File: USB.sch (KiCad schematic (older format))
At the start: 7 parts

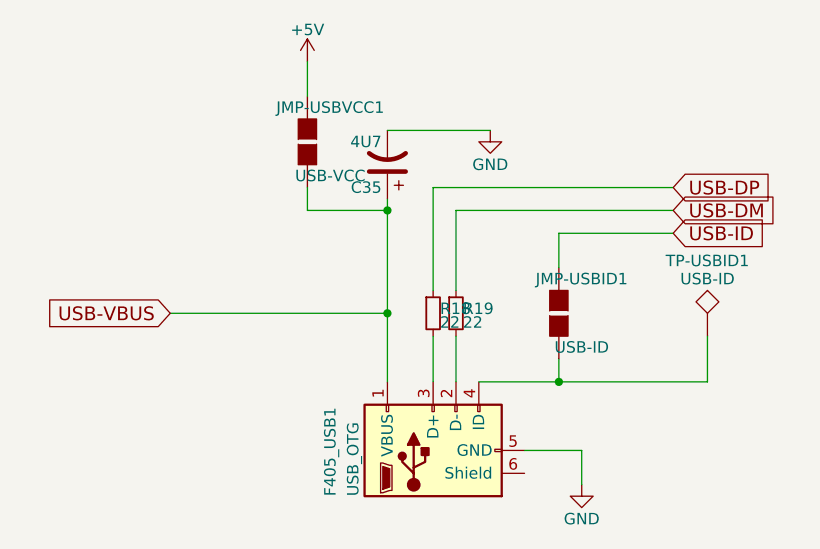
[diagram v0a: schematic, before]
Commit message: tp name fixes
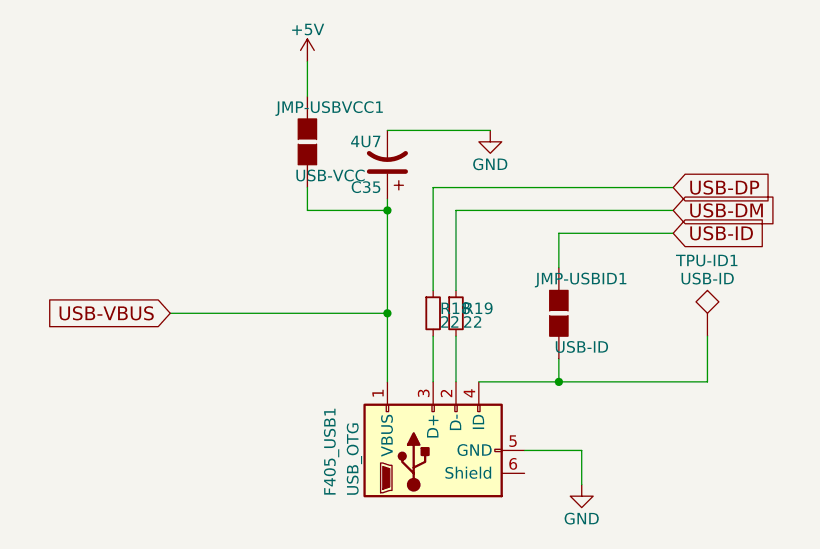
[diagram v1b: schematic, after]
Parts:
- renumbered TP-USBID1 to TPU-ID1
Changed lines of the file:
@@
 $EndComp
 $Comp
-L TEST TP-USBID1
+L TEST TPU-ID1
 U 1 1 5B312B63
 P 7050 3800
-F 0 "TP-USBID1" H 7050 4100 50  0000 C BNN
+F 0 "TPU-ID1" H 7050 4100 50  0000 C BNN
 F 1 "USB-ID" H 7050 4050 50  0000 C CNN
 F 2 "Measurement_Points:Measurement_Point_Round-SMD-Pad_Small" H 7050 3800 50  0001 C CNN

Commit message: Name changes on silk
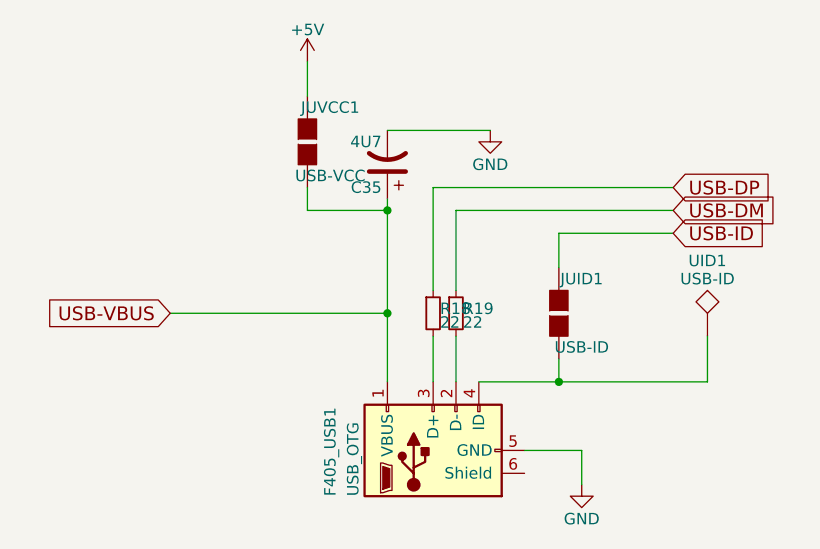
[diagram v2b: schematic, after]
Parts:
- renumbered JMP-USBID1 to JUID1, JMP-USBVCC1 to JUVCC1, TPU-ID1 to UID1
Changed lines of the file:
@@
 $EndComp
 $Comp
-L GND #PWR44
+L GND #PWR043
 U 1 1 5B312B57
 P 6100 2900
-F 0 "#PWR44" H 6100 2650 50  0001 C CNN
+F 0 "#PWR043" H 6100 2650 50  0001 C CNN
 F 1 "GND" H 6100 2750 50  0000 C CNN
 F 2 "" H 6100 2900 50  0001 C CNN
@@
 $EndComp
 $Comp
-L GND #PWR45
+L GND #PWR044
 U 1 1 5B312B5D
 P 6500 4450
-F 0 "#PWR45" H 6500 4200 50  0001 C CNN
+F 0 "#PWR044" H 6500 4200 50  0001 C CNN
 F 1 "GND" H 6500 4300 50  0000 C CNN
 F 2 "" H 6500 4450 50  0001 C CNN
@@
 $EndComp
 $Comp
-L TEST TPU-ID1
+L TEST UID1
 U 1 1 5B312B63
 P 7050 3800
-F 0 "TPU-ID1" H 7050 4100 50  0000 C BNN
+F 0 "UID1" H 7050 4100 50  0000 C BNN
 F 1 "USB-ID" H 7050 4050 50  0000 C CNN
 F 2 "Measurement_Points:Measurement_Point_Round-SMD-Pad_Small" H 7050 3800 50  0001 C CNN
@@
 $EndComp
 $Comp
-L GS2 JMP-USBID1
+L GS2 JUID1
 U 1 1 5B312B6A
 P 6400 3700
-F 0 "JMP-USBID1" H 6500 3850 50  0000 C CNN
+F 0 "JUID1" H 6500 3850 50  0000 C CNN
 F 1 "USB-ID" H 6500 3551 50  0000 C CNN
 F 2 "Connect:GS2" V 6474 3700 50  0001 C CNN
@@
 $EndComp
 $Comp
-L GS2 JMP-USBVCC1
+L GS2 JUVCC1
 U 1 1 5B312B71
 P 5300 2950
-F 0 "JMP-USBVCC1" H 5400 3100 50  0000 C CNN
+F 0 "JUVCC1" H 5400 3100 50  0000 C CNN
 F 1 "USB-VCC" H 5400 2801 50  0000 C CNN
 F 2 "Connect:GS2" V 5374 2950 50  0001 C CNN
@@
 	5850 3150 6900 3150
 $Comp
-L +5V #PWR43
+L +5V #PWR045
 U 1 1 5B114EBC
 P 5300 2600
-F 0 "#PWR43" H 5300 2450 50  0001 C CNN
+F 0 "#PWR045" H 5300 2450 50  0001 C CNN
 F 1 "+5V" H 5300 2740 50  0000 C CNN
 F 2 "" H 5300 2600 50  0001 C CNN

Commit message: Fixed up some mess + IR + USB new footprint + buttons
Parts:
- F405_USB1: footprint gsg-modules:USB-MICROB-FCI-10103592-EXT -> digikey-footprints:USB_Micro_B_Female_10118192
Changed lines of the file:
@@
 F 0 "F405_USB1" H 5650 4750 50  0000 L CNN
 F 1 "USB_OTG" H 5650 4650 50  0000 L CNN
-F 2 "gsg-modules:USB-MICROB-FCI-10103592-EXT" H 6000 4250 50  0001 C CNN
+F 2 "digikey-footprints:USB_Micro_B_Female_10118192" H 6000 4250 50  0001 C CNN
 F 3 "" H 6000 4250 50  0001 C CNN
 	1    5850 4300
@@
 $EndComp
 $Comp
-L GND #PWR44
+L GND #PWR45
 U 1 1 5B312B57
 P 6100 2900
-F 0 "#PWR44" H 6100 2650 50  0001 C CNN
+F 0 "#PWR45" H 6100 2650 50  0001 C CNN
 F 1 "GND" H 6100 2750 50  0000 C CNN
 F 2 "" H 6100 2900 50  0001 C CNN
@@
 $EndComp
 $Comp
-L GND #PWR45
+L GND #PWR46
 U 1 1 5B312B5D
 P 6500 4450
-F 0 "#PWR45" H 6500 4200 50  0001 C CNN
+F 0 "#PWR46" H 6500 4200 50  0001 C CNN
 F 1 "GND" H 6500 4300 50  0000 C CNN
 F 2 "" H 6500 4450 50  0001 C CNN
@@
 	5850 3150 6900 3150
 $Comp
-L +5V #PWR43
+L +5V #PWR44
 U 1 1 5B114EBC
 P 5300 2600
-F 0 "#PWR43" H 5300 2450 50  0001 C CNN
+F 0 "#PWR44" H 5300 2450 50  0001 C CNN
 F 1 "+5V" H 5300 2740 50  0000 C CNN
 F 2 "" H 5300 2600 50  0001 C CNN
